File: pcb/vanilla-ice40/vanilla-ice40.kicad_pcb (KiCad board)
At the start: 4 copper layers, 100 x 62 mm, 110 parts, among them J1 Conn_01x02_Pin, J2 SM04B-SRSS-TBLFSN, J3 FX18-120S-0.8SH, J4 Conn_01x06_Pin, J5 Conn_01x02_Pin, J6 Conn_01x02_Pin, J7 Conn_01x02_Pin, U1 TPS563252DRLR, U2 ICE40HX4K-TQ144, U3 W25X40CLSN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

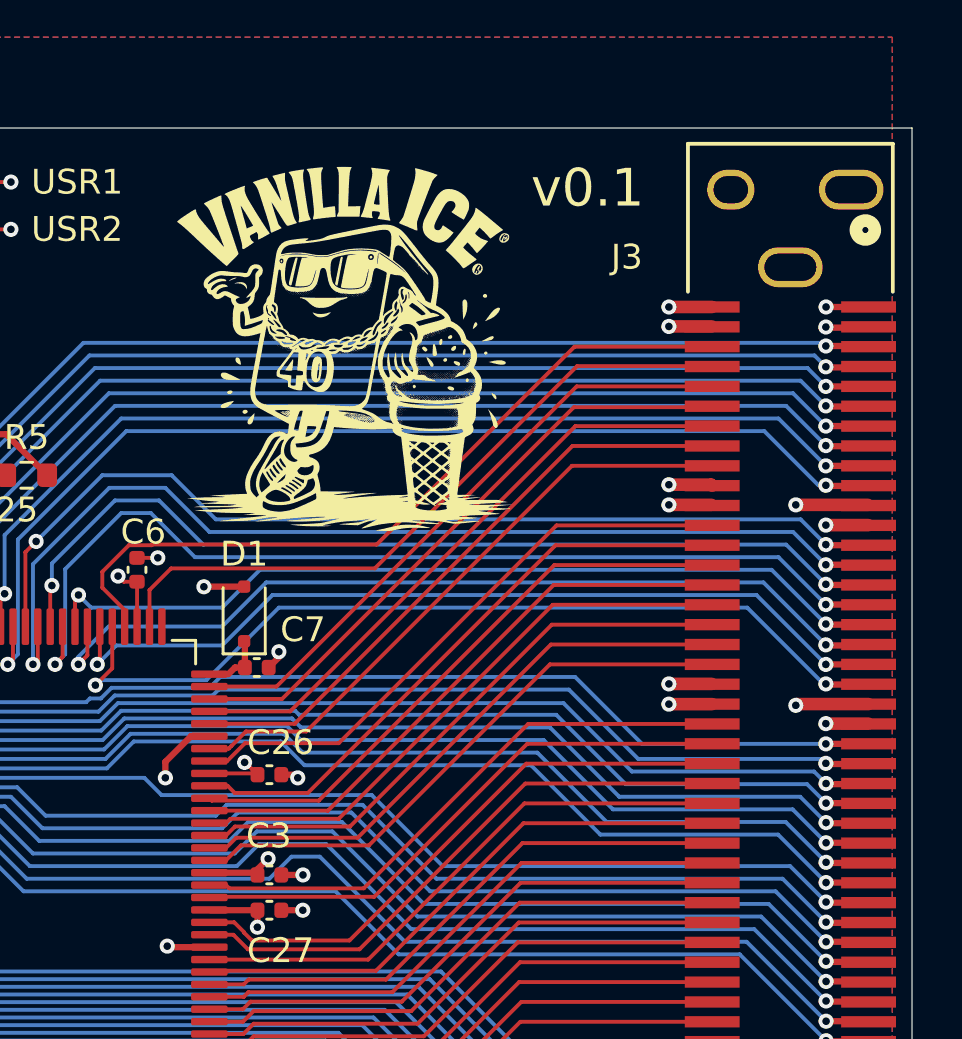
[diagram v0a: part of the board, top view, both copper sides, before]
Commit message: fix 1 off error in fx18 pin layout
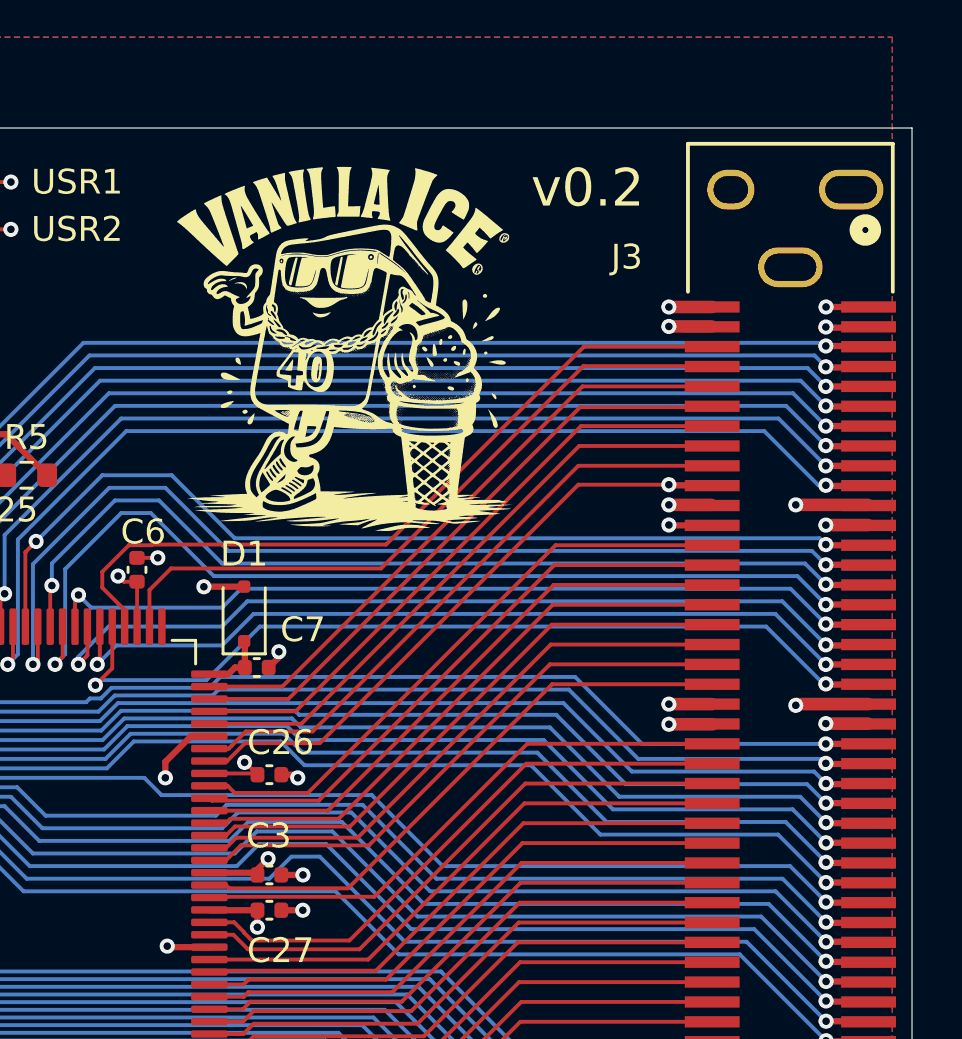
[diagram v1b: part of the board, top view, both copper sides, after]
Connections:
- J3 pad 70: +3V3 -> /IOR_160
- J3 pad 71: GND -> +3V3
- J3 pad 72: /IOR_160 -> GND
- J3 pad 80: +3V3 -> /IOR_139
- J3 pad 81: GND -> +3V3
- J3 pad 82: /IOR_139 -> GND
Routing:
- net GND: track 192.3 -> 188.8 mm
- net /IOR_160: track 24.2 -> 24.9 mm, vias 0 -> 1
- net /IOR_139: track 23.1 -> 23.7 mm
- net /IOT_173: track 34.9 -> 34.3 mm
- net /IOT_172: track 36.1 -> 35.5 mm
- net /IOT_170: track 36.4 -> 35.7 mm
- net /IOT_171: track 35.0 -> 34.4 mm
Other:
- board text added: "v0.2"
- board text removed: "v0.1"

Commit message: [pcb] misc updates prior to ordder
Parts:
- removed 1V2_1, 3V3_1: Red, Diode_SMD:D_0603_1608Metric
- removed R11, R21: 2.2k, Resistor_SMD:R_0603_1608Metric
- R6: value 2.2k -> 5.1k
- moved 5V_1 3.81 mm to (68.7, 32.9)
- moved R6 3.81 mm to (65.3, 32.9), turned to 180 degrees
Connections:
- R6 pad 1: VBUS_5V -> Net-(5V_1-A)
- R6 pad 2: Net-(5V_1-A) -> VBUS_5V
- U1 pad 5: unconnected-(U1-EN-Pad5) -> VBUS_5V
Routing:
- net +1V2: track 213.2 -> 191.7 mm, vias 11 -> 10
- net VBUS_5V: track 37.8 -> 41.0 mm
- net GND: track 188.8 -> 186.6 mm, vias 128 -> 126
- net Net-(3V3_1-A): track 1.79 -> 0.00 mm
- net Net-(1V2_1-A): track 1.79 -> 0.00 mm
- net +3V3: track 130.6 -> 129.3 mm, vias 48 -> 47
- net Net-(U1-PG): track 41.0 -> 41.7 mm
- net /IOR_160: vias 1 -> 0
